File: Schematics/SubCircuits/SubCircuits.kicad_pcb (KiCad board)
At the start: 2 copper layers, 67.8 x 55.5 mm, 60 parts, among them J1 USB-C, J10 MainBoard, J11 O, J12 Prog edge, J13 Output, J2 Batt, J4 Batt_alt, J5 LED, J6 LED, J7 I, J8 I2C_OLED, J9 Prog edge, Q1 BSS138, SW1 PHB2UOATS1A, SW2 RST, SW3 RST, U1 BQ25300, U2 TPS63001, U3 HT7750B, U5 STM32G070K

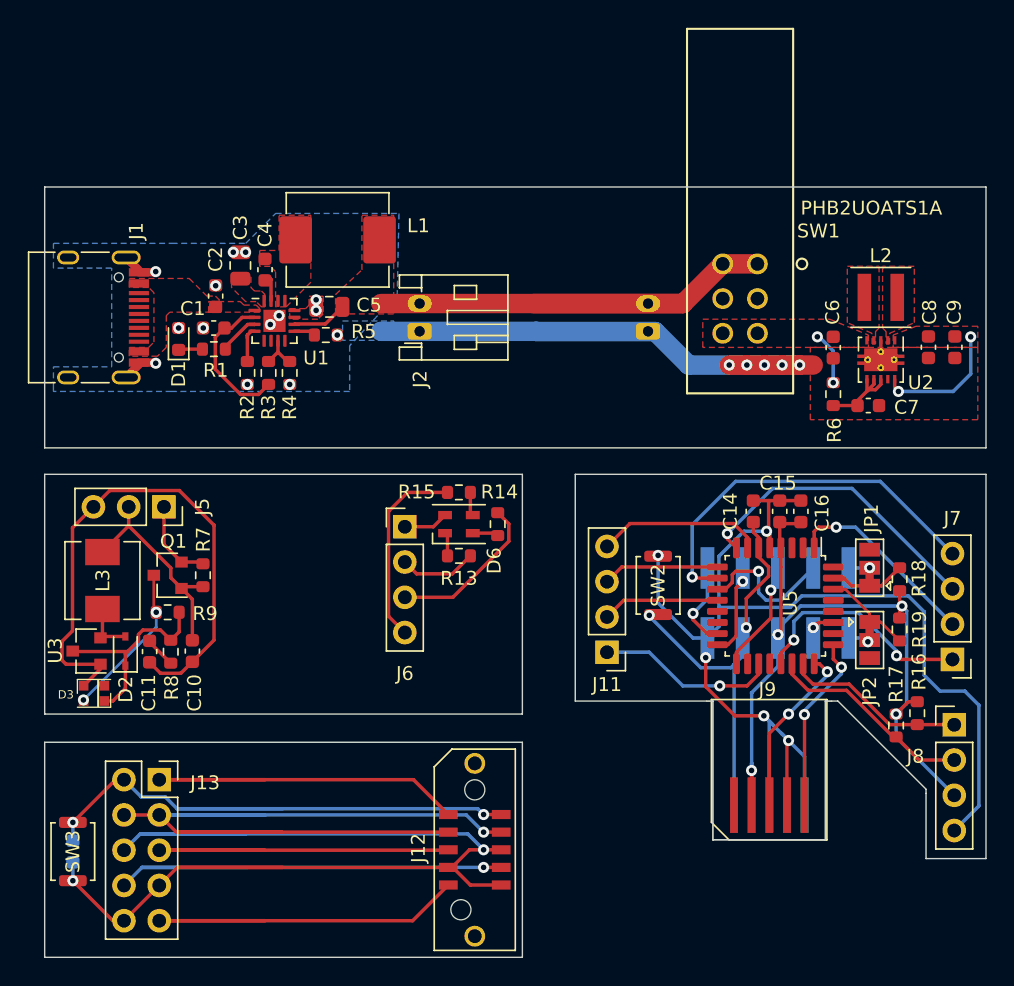
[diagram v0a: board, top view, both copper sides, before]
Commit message: Added defunct subcircuit project
superseded by modular mainboard
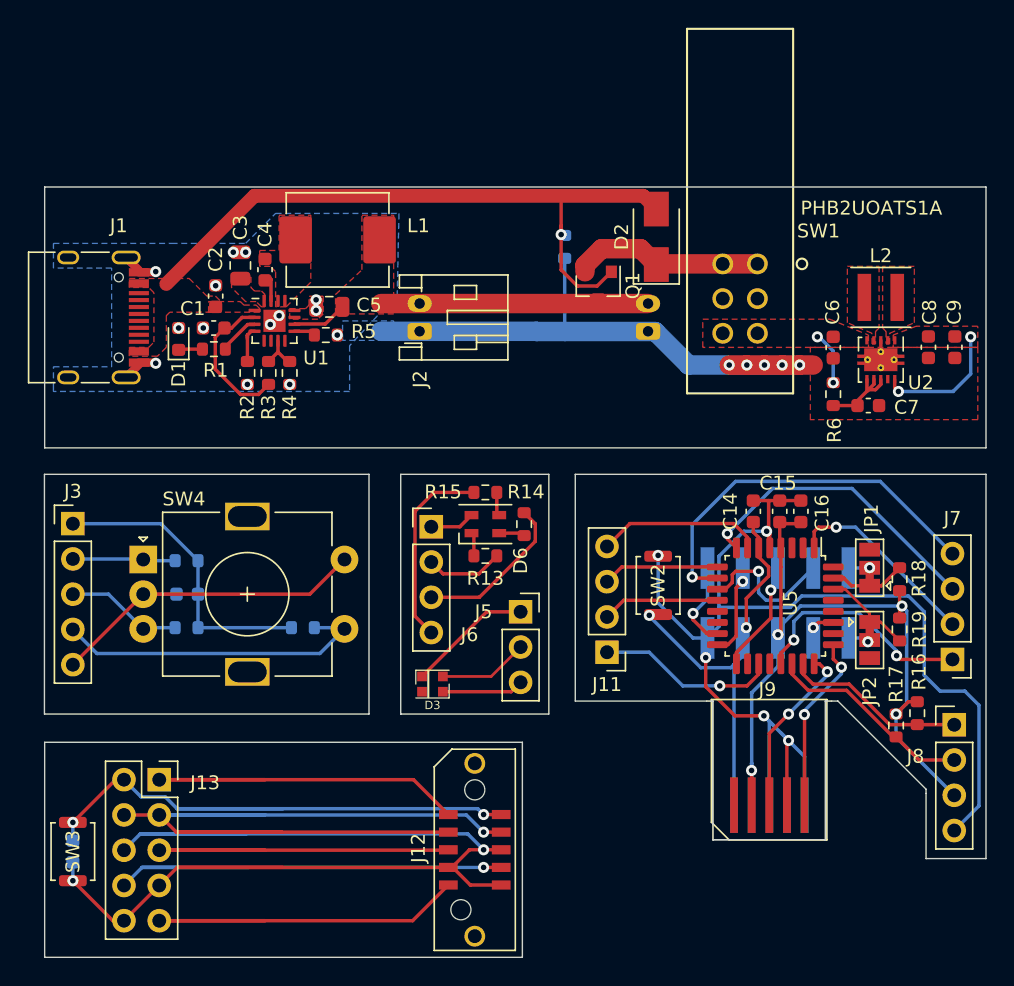
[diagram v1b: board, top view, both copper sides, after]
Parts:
- removed C11: 22u, Capacitor_SMD:C_0603_1608Metric
- removed L3: SWPA5040S, Inductor_SMD:L_Sunlord_MWSA0518_5.4x5.2mm
- removed U3: HT7750B, Package_TO_SOT_SMD:SOT-23
- added J3: Rot, Connector_PinHeader_2.54mm:PinHeader_1x05_P2.54mm_Vertical, F.Cu at (70.4, 71.9)
- added R10: 100k, Resistor_SMD:R_0603_1608Metric, B.Cu at (105.8, 51.9)
- added SW4: Rot, Rotary_Encoder:RotaryEncoder_Alps_EC11E-Switch_Vertical_H20mm, F.Cu at (75.4, 74.5)
- C10: value 47u -> 10u; moved to B.Cu
- C16: value 100n -> 0.1u
- D2: value 1N5817 -> SS24; footprint Diode_SMD:D_SOD-323 -> Diode_SMD:D_SMA
- J11: value O -> Output
- J5: value LED -> ADDR_LED
- J7: value I -> Input
- Q1: value BSS138 -> AO3401A
- R5: value TBD -> 0
- R7, R9: value 10k -> 47k; moved to B.Cu
- R8: value 0.15 -> 47k; moved to B.Cu
- moved D2 48.5 mm to (112.4, 51.2)
- moved Q1 37.4 mm to (108.2, 54.7), turned to -90 degrees
- moved J5 26.8 mm to (102.6, 78.2), turned to 0 degrees
- moved D3 24.4 mm to (96.3, 83.4), turned to 180 degrees
- moved R9 9.81 mm to (86.9, 79.4)
- moved R8 6.66 mm to (78.5, 74.5), turned to 0 degrees
- moved C10 4.11 mm to (78.6, 77.0), turned to 180 degrees
- moved R7 3.96 mm to (78.5, 79.4), turned to 0 degrees
- moved J6 1.91 mm to (96.2, 72.1)
- moved R14 1.91 mm to (102.9, 71.9)
- moved D6 1.90 mm to (100.1, 71.9)
- moved R13 1.90 mm to (100.1, 74.2)
- moved R15 1.90 mm to (100.1, 69.6)
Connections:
- net /Power/BATT_SW renamed /Power/POWER_SW
- net /STM33/NRST renamed /STM33 Programmer/NRST
- net /STM33/RX renamed /STM33 Programmer/RX
- net /STM33/SWC renamed /STM33 Programmer/SWC
- net /STM33/SWD renamed /STM33 Programmer/SWD
- net /STM33/TX renamed /STM33 Programmer/TX
- D2 pad 1: /LED Boost/5V_local -> /Power/POWER
- D2 pad 2: Net-(D2-Pad2) -> VBUS
- D3 pad 1: /LED Boost/5V_local -> /LED Boost/3.3V_local
- D3 pad 2: unconnected-(D3-Pad2) -> (no net)
- D3 pad 3: GND -> /LED Boost/GND_local
- J5 pad 1: /LED Boost/DIN_LV -> /LED Boost/3.3V_local
- J5 pad 2: +3V3 -> /LED Boost/DIN
- J5 pad 3: GND -> /LED Boost/GND_local
- Q1 pad 1: +3V3 -> VBUS
- Q1 pad 2: /LED Boost/DIN_LV -> /Power/POWER
- Q1 pad 3: /LED Boost/DIN -> +BATT
- R7 pad 1: /LED Boost/DIN_LV -> /Rotary encoder/R_B
- R8 pad 1: /LED Boost/5V_local -> /Rotary encoder/R_A
- R8 pad 2: Net-(C11-Pad1) -> +3V3
- R9 pad 1: /LED Boost/5V_local -> /Rotary encoder/R_SW
- R9 pad 2: /LED Boost/DIN -> +3V3
- SW1 pad 1: +BATT -> /Power/POWER
- SW1 pad 4: +BATT -> /Power/POWER
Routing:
- net VBUS: track 0.00 -> 49.5 mm, vias 0 -> 1
- net /Rotary encoder/R_SW: track 0.00 -> 23.2 mm
- net +BATT: track 43.1 -> 23.2 mm
- net /LED Boost/5V_local: track 15.2 -> 0.00 mm
- net /Power/POWER: track 0.00 -> 13.9 mm
- net GND: track 259.5 -> 248.5 mm
- net /LED Boost/3.3V_local: track 3.24 -> 12.3 mm
- net /Rotary encoder/R_B: track 0.00 -> 8.44 mm
- net /Rotary encoder/R_A: track 0.00 -> 7.42 mm
- net /LED Boost/DIN_LV: track 6.10 -> 0.00 mm
- net +3V3: track 145.4 -> 151.3 mm
- net /LED Boost/GND_local: track 0.00 -> 5.88 mm
- net /LED Boost/DIN: track 11.3 -> 6.48 mm, vias 2 -> 0
- net Net-(D2-Pad2): track 3.97 -> 0.00 mm
- net Net-(C11-Pad1): track 2.24 -> 0.00 mm
- added copper zone on F.Cu, net (none)
- removed copper zone on F.Cu, net /Power/POWER_SW
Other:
- outline, holes or cut-outs redrawn
